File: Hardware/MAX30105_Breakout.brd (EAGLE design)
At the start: 20.3 x 22.9 mm, 27 parts, among them Q1 200mA/50V, Q2 200mA/50V, U1 1.8V/100mA, U2 MAX30105

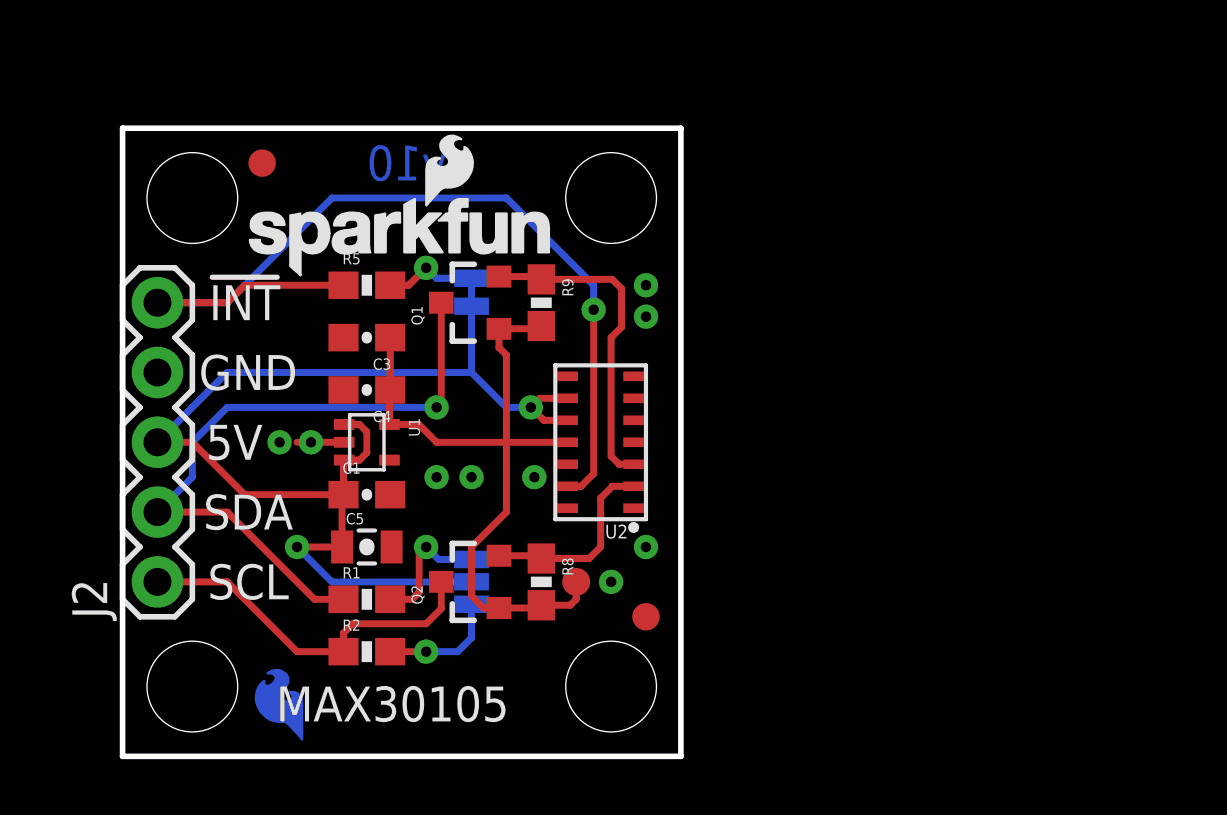
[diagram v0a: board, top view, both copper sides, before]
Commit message: adding silk labelling
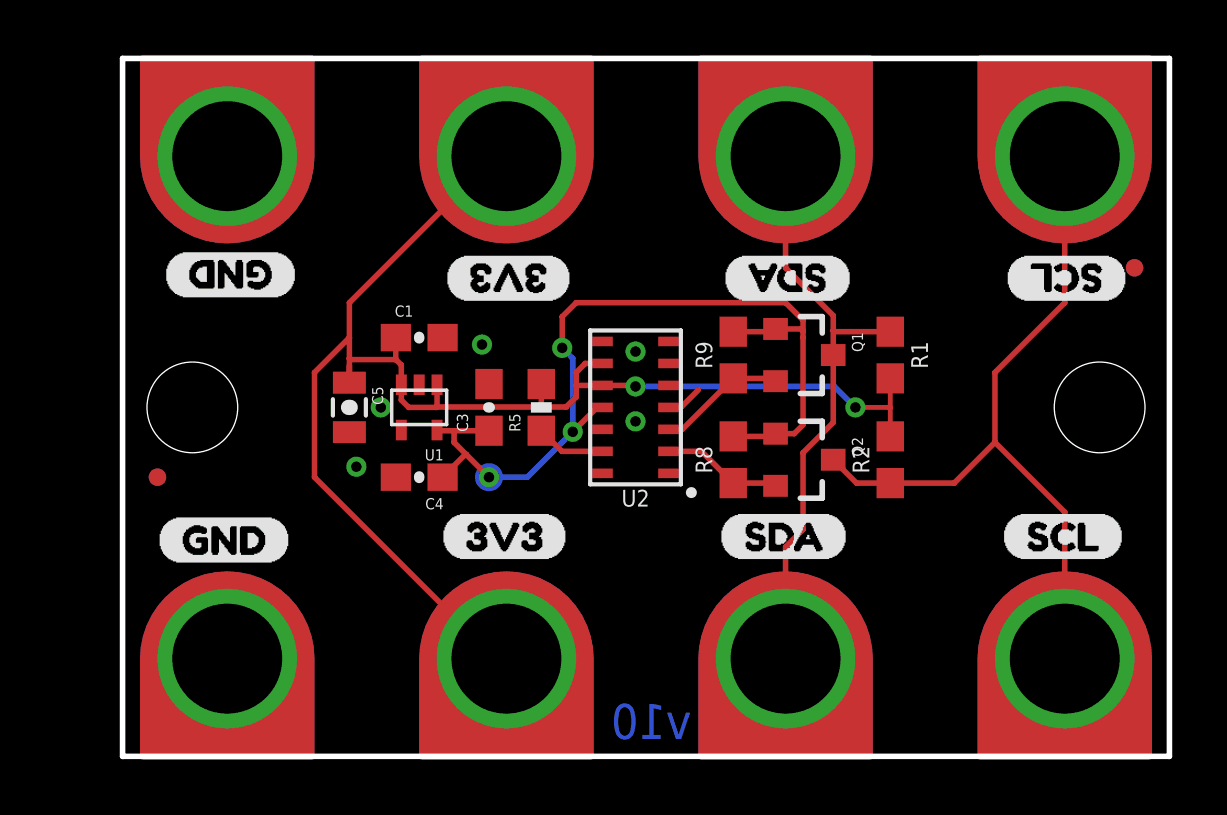
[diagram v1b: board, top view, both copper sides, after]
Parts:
- removed JP2: INT, SparkFun-Passives:PAD-JUMPER-2-NC_BY_TRACE_YES_SILK
- removed JP3: PU, SparkFun-Passives:PAD-JUMPER-3-3OF3_NC_BY_TRACE_YES_SILK_FULL_BOX
- removed LOGO1: SFE_LOGO_NAME_FLAME.1_INCH, SparkFun-Aesthetics:SFE_LOGO_NAME_FLAME_.1
- removed LOGO4: SFE_LOGO_FLAME.1EXP, SparkFun-Aesthetics:SFE_LOGO_FLAME_COPPER_EXPOSED_.1
- removed STANDOFF1, STANDOFF4: STAND-OFF, SparkFun-Electromechanical:STAND-OFF
- added FID3, FID4: FIDUCIALUFIDUCIAL, SparkFun-Aesthetics:FIDUCIAL-MICRO
- added J1, J3, J4, J5, J6, J7, J8: GATORGATOR_MINI, SparkFun-Connectors:GATOR_MINI
- added U$1, U$13, U$5, U$9: (no value), buzzard_labels (2):GND0
- added U$10, U$14, U$2, U$6: (no value), buzzard_labels (2):3V33
- added U$11, U$15, U$3, U$7: (no value), buzzard_labels (2):SDA2
- added U$12, U$16, U$4, U$8: (no value), buzzard_labels (2):SCL1
- FID1, FID2: value FIDUCIAL1X2 -> FIDUCIALUFIDUCIAL; device SparkFun-Aesthetics:FIDUCIAL-1X2 -> SparkFun-Aesthetics:FIDUCIAL-MICRO
- J2: value (none) -> GATORGATOR_MINI; device SparkFun-Connectors:1X05 -> SparkFun-Connectors:GATOR_MINI
- R1, R2: value 4.7K -> 10k; device SparkFun-Resistors:0603-RES -> SparkFun-Resistors:0603
- R8, R9: value 4.7K -> 2.2k; device SparkFun-Resistors:0603-RES -> SparkFun-Resistors:0603
- U2: value MAX30105 -> 30102
- moved FID1 21.8 mm to (36.8, 17.8)
- moved R1 21.0 mm to (27.9, 14.6), turned to 270 degrees
- moved STANDOFF2 20.5 mm to (35.6, 12.7)
- moved R2 20.3 mm to (27.9, 10.8), turned to 90 degrees
- moved J2 13.0 mm to (14.0, 3.81), turned to 0 degrees
- moved Q2 12.9 mm to (24.8, 10.8), turned to 270 degrees
- moved Q1 12.2 mm to (24.8, 14.6), turned to 270 degrees
- moved FID2 12.0 mm to (1.27, 10.2), flipped to the bottom
- moved STANDOFF3 10.2 mm to (2.54, 12.7)
- moved R8 8.28 mm to (22.2, 10.8), turned to 90 degrees
- moved R5 7.75 mm to (15.2, 12.7), turned to 90 degrees
- moved R9 7.24 mm to (22.2, 14.6), turned to 90 degrees
- moved C1 6.02 mm to (10.8, 15.2)
- moved C3 5.12 mm to (13.3, 12.7), turned to 90 degrees
- moved C5 5.12 mm to (8.26, 12.7), turned to 270 degrees
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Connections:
- removed net 5V: C1.1, C5.1, J2.3, JP2.2, JP3.2, U1.1, U1.3, U2.10, U2.9
- removed net N$1: JP2.1, R5.2
- removed net N$2: JP3.1, R2.2
- removed net N$3: JP3.3, R1.2
- new net 3.3V: C1.1, C5.1, J2.P$2, J6.P$2, R1.2, R2.2, R5.2, U1.1, U1.3, U2.10, U2.9
- net !INT: no longer J2.5
- net GND: now also J1.P$2, J5.P$2; no longer J2.4
- net SCL: now also J4.P$2, J8.P$2; no longer J2.1
- net SDA: now also J3.P$2, J7.P$2; no longer J2.2
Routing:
- net 3.3V: track 0.00 -> 55.3 mm, vias 0 -> 2
- net 5V: track 42.5 -> 0.00 mm, vias 2 -> 0
- net !INT: track 33.8 -> 2.54 mm, vias 1 -> 0
- net SCL: track 13.4 -> 27.2 mm
- net 1.8V: track 26.6 -> 33.8 mm, vias 0 -> 3
- net LV_SDA: track 11.8 -> 4.71 mm
- net N$3: track 4.76 -> 0.00 mm, vias 1 -> 0
- net N$2: track 4.39 -> 0.00 mm, vias 1 -> 0
- net N$1: track 3.38 -> 0.00 mm, vias 1 -> 0
- net SDA: track 24.4 -> 21.7 mm, vias 1 -> 0
- net LV_SCL: track 7.07 -> 4.42 mm
- net GND: track 1.71 -> 1.35 mm, vias 9 -> 5
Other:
- board size 20.3 x 22.9 mm -> 38.1 x 25.4 mm
- board text added: "A. England"
- board text removed: "!INT"
- board text removed: "5V"
- board text removed: "Clears 4-40 Screw"
- board text removed: "GND"
- board text removed: "INT"
- board text removed: "MAX30105"
- board text removed: "MAX30105 Particle Sensor"
- board text removed: "N. Seidle"
- board text removed: "PU"
- board text removed: "SCL"
- board text removed: "SDA"

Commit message: adding protection circuitry
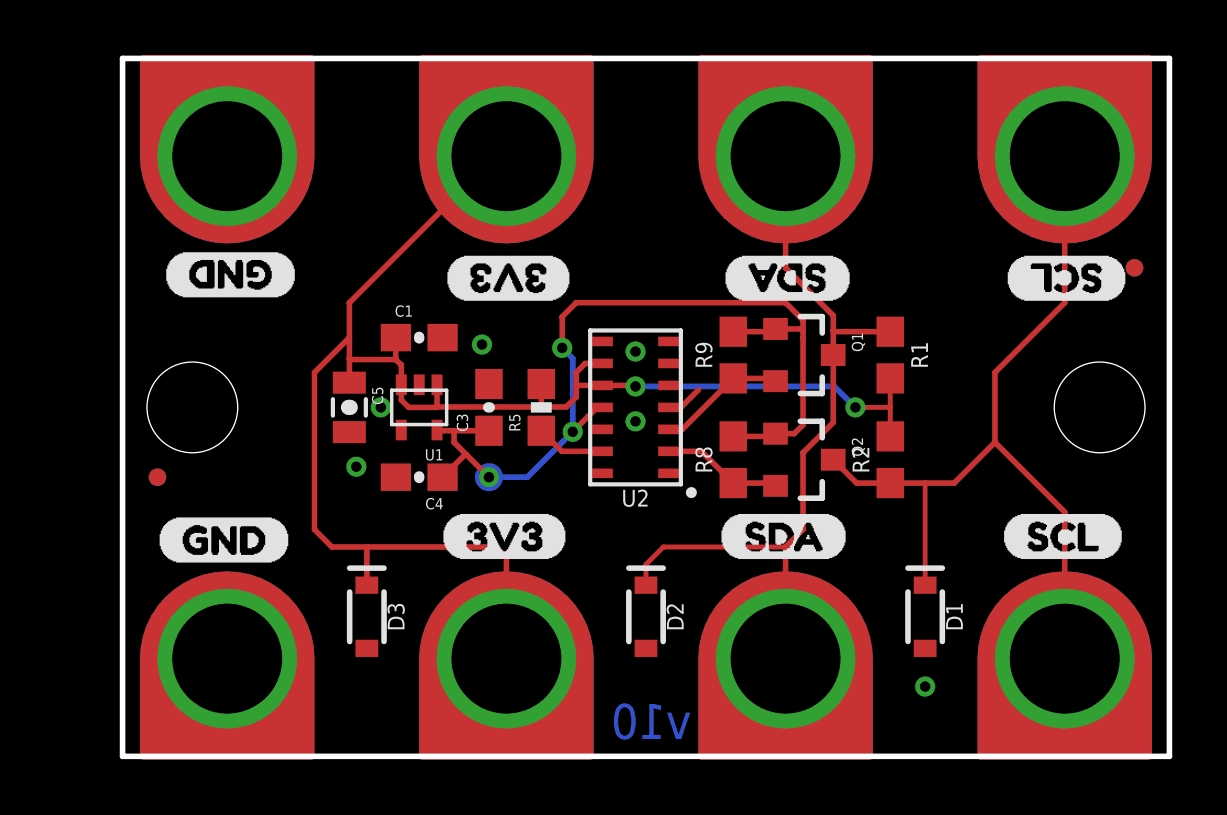
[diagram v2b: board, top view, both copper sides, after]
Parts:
- added D1, D2, D3: 3.6V, SparkFun-DiscreteSemi:SOD-323
- Q1, Q2: device SparkFun-DiscreteSemi:SOT23-3 -> SparkFun-DiscreteSemi:SOT23-3@1
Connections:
- net 3.3V: now also D3.C
- net GND: now also D1.A, D2.A, D3.A
- net SCL: now also D1.C
- net SDA: now also D2.C
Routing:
- net SDA: track 21.7 -> 27.8 mm
- net 3.3V: track 55.3 -> 60.1 mm
- net SCL: track 27.2 -> 31.0 mm
- net GND: vias 5 -> 6

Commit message: finalizing silk and schematic before design review
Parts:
- added U$17: (no value), SparkFun-Aesthetics:SFE_LOGO_FLAME_.2
- added U$18: (no value), GatorBit_Final_for_Silk#01#png (2):GATORBIT_FINAL_FOR_SILK#01#PNG
- added U$19: (no value), SparkFun-Aesthetics:SFE_LOGO_NAME_FLAME_.1
- added U$20: (no value), buzzard_labels (4):GATOR#PARTICLE2
- added U$21: (no value), GatorBit_Final_for_Silk#01#png (3):GATORBIT_FINAL_FOR_SILK#01#PNG
- moved U2 0.38 mm to (19.1, 12.7)
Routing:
- net LV_SDA: track 4.71 -> 5.61 mm
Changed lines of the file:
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@@
 <?xml version="1.0" encoding="utf-8"?>
 <!DOCTYPE eagle SYSTEM "eagle.dtd">
-<eagle version="9.3.1">
+<eagle version="9.1.0">
 <drawing>
 <settings>
@@
 <attribute name="VALUE" x="24.5745" y="11.811" size="0.4064" layer="27" rot="R270"/>
 </element>
-<element name="U2" library="SparkFun-Sensors" package="OLGA-14" value="30102" x="18.669" y="12.7" smashed="yes" rot="R180">
-<attribute name="NAME" x="18.669" y="9.7" size="0.6096" layer="25" font="vector" ratio="20" rot="R180" align="bottom-center"/>
-<attribute name="PROD_ID" value="IC-14316" x="18.669" y="12.7" size="1.778" layer="27" rot="R180" display="off"/>
-<attribute name="VALUE" x="18.669" y="15.748" size="0.6096" layer="27" font="vector" ratio="20" rot="R180" align="top-center"/>
+<element name="U2" library="SparkFun-Sensors" package="OLGA-14" value="30102" x="19.05" y="12.7" smashed="yes" rot="R180">
+<attribute name="NAME" x="19.05" y="9.7" size="0.6096" layer="25" font="vector" ratio="20" rot="R180" align="bottom-center"/>
+<attribute name="PROD_ID" value="IC-14316" x="19.05" y="12.7" size="1.778" layer="27" rot="R180" display="off"/>
+<attribute name="VALUE" x="19.05" y="15.748" size="0.6096" layer="27" font="vector" ratio="20" rot="R180" align="top-center"/>
 </element>
 <element name="FRAME1" library="SparkFun-Aesthetics" package="CREATIVE_COMMONS" value="FRAME-LETTER" x="-2.54" y="-16.51" smashed="yes"/>
@@
 <attribute name="VALUE" x="8.128" y="5.08" size="0.6096" layer="27" font="vector" ratio="20" rot="R270" align="top-center"/>
 </element>
+<element name="U$17" library="SparkFun-Aesthetics" package="SFE_LOGO_FLAME_.2" value="" x="31.242" y="12.573"/>
+<element name="U$18" library="GatorBit_Final_for_Silk#01#png (2)" package="GATORBIT_FINAL_FOR_SILK#01#PNG" value="" x="19.05" y="17.78"/>
+<element name="U$19" library="SparkFun-Aesthetics" package="SFE_LOGO_NAME_FLAME_.1" value="" x="19.05" y="15.24" rot="MR0"/>
+<element name="U$20" library="buzzard_labels (4)" package="GATOR#PARTICLE2" value="" x="24.765" y="12.827" rot="MR0"/>
+<element name="U$21" library="GatorBit_Final_for_Silk#01#png (3)" package="GATORBIT_FINAL_FOR_SILK#01#PNG" value="" x="18.923" y="10.16" rot="MR0"/>
 </elements>
 <signals>
@@
 <via x="9.398" y="12.7" extent="1-16" drill="0.381"/>
 <via x="13.081" y="14.986" extent="1-16" drill="0.381"/>
-<wire x1="19.869" y1="12.7" x2="20.32" y2="12.7" width="0.2032" layer="1"/>
-<wire x1="20.32" y1="12.7" x2="20.955" y2="13.335" width="0.2032" layer="1"/>
-<via x="18.669" y="12.192" extent="1-16" drill="0.381"/>
+<wire x1="20.25" y1="12.7" x2="20.701" y2="12.7" width="0.2032" layer="1"/>
+<wire x1="20.701" y1="12.7" x2="21.336" y2="13.335" width="0.2032" layer="1"/>
+<via x="19.05" y="12.192" extent="1-16" drill="0.381"/>
 <via x="8.509" y="10.541" extent="1-16" drill="0.381"/>
-<via x="18.669" y="14.732" extent="1-16" drill="0.381"/>
+<via x="19.05" y="14.732" extent="1-16" drill="0.381"/>
 <contactref element="D1" pad="A"/>
 <contactref element="D2" pad="A"/>
@@
 <wire x1="22.225" y1="9.945" x2="23.665" y2="9.945" width="0.2032" layer="1"/>
 <wire x1="23.665" y1="9.945" x2="23.765" y2="9.845" width="0.2032" layer="1"/>
-<wire x1="19.869" y1="11.1" x2="21.07" y2="11.1" width="0.2032" layer="1"/>
-<wire x1="21.07" y1="11.1" x2="22.225" y2="9.945" width="0.2032" layer="1"/>
+<wire x1="22.225" y1="10.326" x2="22.225" y2="9.945" width="0.2032" layer="1"/>
+<wire x1="20.25" y1="11.1" x2="21.07" y2="11.1" width="0.1778" layer="1"/>
+<wire x1="21.07" y1="11.1" x2="22.225" y2="9.945" width="0.1778" layer="1"/>
 </signal>
 <signal name="LV_SDA">
@@
 <wire x1="22.225" y1="13.755" x2="23.665" y2="13.755" width="0.2032" layer="1"/>
 <wire x1="23.665" y1="13.755" x2="23.765" y2="13.655" width="0.2032" layer="1"/>
-<wire x1="19.869" y1="11.9" x2="20.37" y2="11.9" width="0.2032" layer="1"/>
-<wire x1="20.37" y1="11.9" x2="22.225" y2="13.755" width="0.2032" layer="1"/>
+<wire x1="20.25" y1="11.9" x2="20.32" y2="11.9" width="0.2032" layer="1"/>
+<wire x1="20.32" y1="11.9" x2="20.751" y2="11.9" width="0.2032" layer="1"/>
+<wire x1="22.225" y1="13.374" x2="22.225" y2="13.755" width="0.2032" layer="1"/>
+<wire x1="20.32" y1="11.9" x2="20.79" y2="11.9" width="0.1778" layer="1"/>
+<wire x1="21.59" y1="12.7" x2="21.971" y2="12.7" width="0.1778" layer="1"/>
+<wire x1="21.971" y1="12.7" x2="22.225" y2="12.954" width="0.1778" layer="1"/>
+<wire x1="22.225" y1="12.954" x2="22.225" y2="13.755" width="0.1778" layer="1"/>
+<wire x1="20.79" y1="11.9" x2="21.59" y2="12.7" width="0.1778" layer="1"/>
 </signal>
 <signal name="3.3V">
@@
 <wire x1="11.445" y1="12.715" x2="11.43" y2="12.7" width="0.2032" layer="1"/>
 <wire x1="11.445" y1="13.525" x2="11.445" y2="12.715" width="0.2032" layer="1"/>
-<wire x1="17.469" y1="14.3" x2="16.84" y2="14.3" width="0.2032" layer="1"/>
-<wire x1="16.84" y1="14.3" x2="16.51" y2="13.97" width="0.2032" layer="1"/>
-<wire x1="17.469" y1="13.5" x2="16.51" y2="13.5" width="0.2032" layer="1"/>
-<wire x1="16.51" y1="13.97" x2="16.51" y2="13.5" width="0.2032" layer="1"/>
+<wire x1="17.85" y1="14.3" x2="17.78" y2="14.3" width="0.2032" layer="1"/>
+<wire x1="17.85" y1="13.5" x2="16.51" y2="13.5" width="0.2032" layer="1"/>
+<wire x1="16.51" y1="13.5" x2="16.51" y2="13.97" width="0.2032" layer="1"/>
 <wire x1="11.445" y1="12.715" x2="15.24" y2="12.715" width="0.2032" layer="1"/>
 <wire x1="15.24" y1="12.715" x2="16.144" y2="12.715" width="0.2032" layer="1"/>
@@
 <via x="26.67" y="12.7" extent="1-16" drill="0.381"/>
 <wire x1="26.67" y1="12.7" x2="25.908" y2="13.462" width="0.2032" layer="16"/>
-<wire x1="25.908" y1="13.462" x2="18.669" y2="13.462" width="0.2032" layer="16"/>
-<via x="18.669" y="13.462" extent="1-16" drill="0.381"/>
-<wire x1="18.669" y1="13.462" x2="18.631" y2="13.5" width="0.2032" layer="1"/>
-<wire x1="18.631" y1="13.5" x2="17.469" y2="13.5" width="0.2032" layer="1"/>
+<wire x1="25.908" y1="13.462" x2="19.05" y2="13.462" width="0.2032" layer="16"/>
+<via x="19.05" y="13.462" extent="1-16" drill="0.381"/>
+<wire x1="19.05" y1="13.462" x2="19.012" y2="13.5" width="0.2032" layer="1"/>
+<wire x1="19.012" y1="13.5" x2="17.85" y2="13.5" width="0.2032" layer="1"/>
 <wire x1="13.97" y1="21.844" x2="13.589" y2="21.844" width="0.2032" layer="1"/>
 <wire x1="8.255" y1="13.6" x2="8.255" y2="14.478" width="0.2032" layer="1"/>
@@
 <wire x1="8.89" y1="7.62" x2="13.589" y2="7.62" width="0.2032" layer="1"/>
 <wire x1="8.89" y1="6.23" x2="8.89" y2="7.62" width="0.2032" layer="1"/>
+<wire x1="16.51" y1="13.97" x2="16.84" y2="14.3" width="0.2032" layer="1"/>
+<wire x1="16.84" y1="14.3" x2="17.85" y2="14.3" width="0.2032" layer="1"/>
 </signal>
 <signal name="1.8V">
@@
 <contactref element="TP1" pad="P$1"/>
 <wire x1="11.445" y1="11.875" x2="11.445" y2="11.669" width="0.2032" layer="1"/>
-<wire x1="17.469" y1="12.7" x2="17.272" y2="12.7" width="0.2032" layer="1"/>
-<wire x1="17.272" y1="12.7" x2="16.383" y2="11.811" width="0.2032" layer="1"/>
+<wire x1="17.85" y1="12.7" x2="17.653" y2="12.7" width="0.2032" layer="1"/>
+<wire x1="17.653" y1="12.7" x2="16.764" y2="11.811" width="0.2032" layer="1"/>
 <via x="16.383" y="11.811" extent="1-16" drill="0.381"/>
 <wire x1="16.383" y1="11.811" x2="14.732" y2="10.16" width="0.2032" layer="16"/>
@@
 <wire x1="23.765" y1="15.555" x2="24.704" y2="15.555" width="0.2032" layer="1"/>
 <wire x1="24.704" y1="15.555" x2="24.765" y2="15.494" width="0.2032" layer="1"/>
+<wire x1="16.764" y1="11.811" x2="16.383" y2="11.811" width="0.2032" layer="1"/>
 </signal>
 <signal name="!INT">
 <contactref element="R5" pad="1"/>
 <contactref element="U2" pad="13"/>
-<wire x1="17.469" y1="11.1" x2="15.99" y2="11.1" width="0.2032" layer="1"/>
+<wire x1="17.85" y1="11.1" x2="15.99" y2="11.1" width="0.2032" layer="1"/>
 <wire x1="15.99" y1="11.1" x2="15.24" y2="11.85" width="0.2032" layer="1"/>
 </signal>

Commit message: engineer run of checklist
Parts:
- removed U$18: (no value), GatorBit_Final_for_Silk#01#png (2):GATORBIT_FINAL_FOR_SILK#01#PNG
- added D4: RED, SparkFun-LED:LED-0603
- added Q3: 2.5A/30V/105mΩ, SparkFun-DiscreteSemi:SOT23-3
- added R3, R4: 10k, SparkFun-Resistors:0603
- added U$22: (no value), buzzard_labels (5):PWR0
- C1, C3, C4: device SparkFun-Capacitors:0603-CAP -> SparkFun-Capacitors:0603
- C5: value 10uF/10V -> 10uF; device SparkFun-Capacitors:0805-CAP -> SparkFun-Capacitors:0603
- R5: value 4.7K -> 4.7k; device SparkFun-Resistors:0603-RES -> SparkFun-Resistors:0603
- moved FID2 3.86 mm to (0.64, 6.35)
- moved FID3 3.86 mm to (0.64, 6.35)
- moved D3 2.68 mm to (10.3, 7.37)
- moved FID1 1.42 mm to (37.5, 19.1)
- moved FID4 1.42 mm to (37.5, 19.1)
- moved D2 1.27 mm to (19.1, 3.81)
- moved U$13 0.25 mm to (6.10, 7.87)
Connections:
- new net N$1: D3.A, Q3.1, R3.2
- new net N$2: J2.P$2, J6.P$2, Q3.3
- new net N$3: D4.C, R4.2
- net 3.3V: now also D4.A, Q3.2; no longer J2.P$2, J6.P$2
- net GND: now also R3.1, R4.1; no longer D3.A
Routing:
- net N$2: track 0.00 -> 30.6 mm
- net 3.3V: track 60.5 -> 55.4 mm
- net N$1: track 0.00 -> 4.71 mm
- net N$3: track 0.00 -> 2.69 mm
- net SDA: track 27.8 -> 29.4 mm
- net 1.8V: track 34.2 -> 33.6 mm
